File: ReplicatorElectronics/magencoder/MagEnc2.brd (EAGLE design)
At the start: 34.3 x 25.4 mm, 13 parts, among them J1 SBH11-PBPC-D07-ST-BK, J2 70553-0037, T1 MMBT2222A

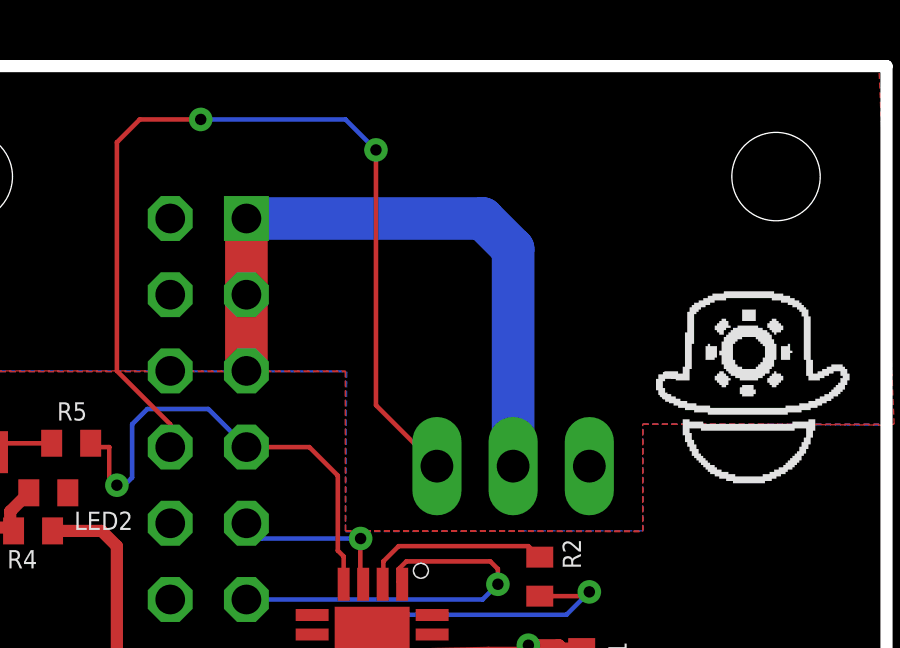
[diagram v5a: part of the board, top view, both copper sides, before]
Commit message: 2/10/13: Updated Encoder Board to include level translation. ~1 hour
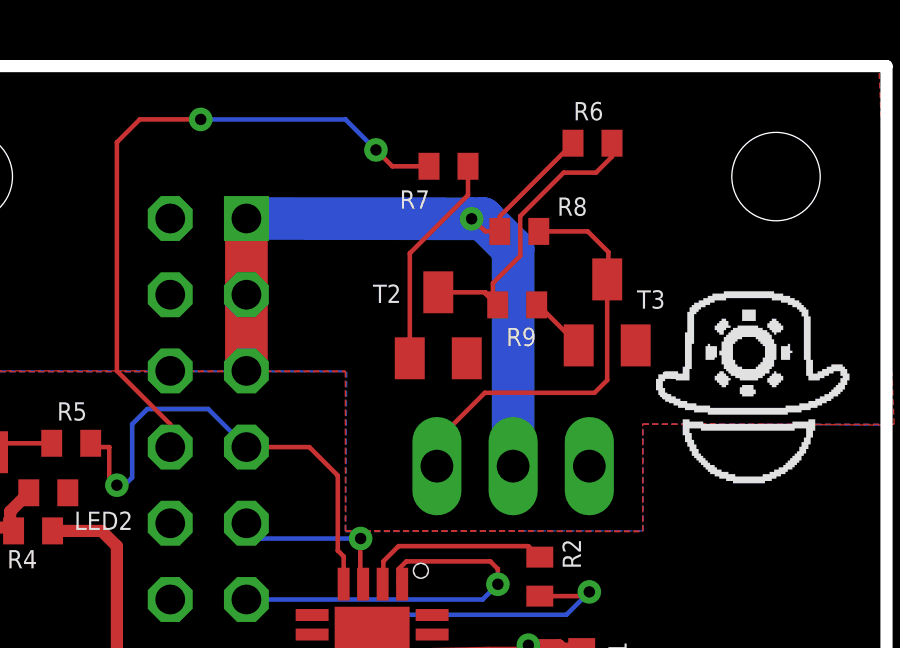
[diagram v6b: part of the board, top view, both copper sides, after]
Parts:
- added R6, R7, R8, R9: 1K, resistor:R0402
- added T2, T3: MMBT2222A, transistor:SOT23-BEC
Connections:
- new net 5V_SERVO_CTRL: J2.3, R8.2, T3.C
- new net CSN1: R6.2, R9.2, T2.C
- new net N$6: R7.1, T2.B
- new net N$8: R9.1, T3.B
- net 5V_SERVO: now also R6.1, R8.1
- net GND: now also T2.E, T3.E
- net SERVO_CTRL: now also R7.2; no longer J2.3
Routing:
- net 5V_SERVO_CTRL: track 0.00 -> 14.3 mm
- net CSN1: track 0.00 -> 10.3 mm
- net SERVO_CTRL: track 31.7 -> 22.3 mm
- net N$6: track 0.00 -> 7.22 mm
- net 5V_SERVO: track 21.6 -> 26.7 mm, vias 0 -> 1
- net N$8: track 0.00 -> 1.96 mm
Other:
- board text added: "Rev. 9"
- board text removed: "Rev. 8"
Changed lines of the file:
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@@
 <?xml version="1.0" encoding="utf-8"?>
 <!DOCTYPE eagle SYSTEM "eagle.dtd">
-<eagle version="6.2">
+<eagle version="6.1">
 <drawing>
 <settings>
@@
 <rectangle x1="27.178" y1="18.288" x2="34.29" y2="25.4" layer="42"/>
 <rectangle x1="27.178" y1="0" x2="34.29" y2="7.112" layer="42"/>
-<text x="28.448" y="9.017" size="0.6096" layer="101" font="vector">Rev. 8</text>
+<text x="28.448" y="9.017" size="0.6096" layer="101" font="vector">Rev. 9</text>
 <text x="25.273" y="8.128" size="0.6096" layer="101" font="vector">Francesco Bivona</text>
 <text x="44.069" y="6.096" size="0.6096" layer="101" font="vector">Mounting holes are 4-40 (0.116")</text>
@@
 <attribute name="NAME" x="24.892" y="3.429" size="0.6096" layer="25" font="vector" rot="R270"/>
 </element>
+<element name="T2" library="transistor" package="SOT23-BEC" value="MMBT2222A" x="19.35" y="16.76" smashed="yes">
+<attribute name="NAME" x="17.175" y="17.505" size="0.6096" layer="25" font="vector"/>
+</element>
+<element name="R6" library="resistor" package="R0402" value="1K" x="24.49" y="22.83" smashed="yes">
+<attribute name="NAME" x="23.855" y="23.592" size="0.6096" layer="25" font="vector"/>
+</element>
+<element name="R7" library="resistor" package="R0402" value="1K" x="19.69" y="22.06" smashed="yes" rot="R180">
+<attribute name="NAME" x="19.065" y="21.258" size="0.6096" layer="25" font="vector" rot="R180"/>
+</element>
+<element name="T3" library="transistor" package="SOT23-BEC" value="MMBT2222A" x="24.98" y="17.19" smashed="yes">
+<attribute name="NAME" x="25.975" y="17.315" size="0.6096" layer="25" font="vector"/>
+</element>
+<element name="R8" library="resistor" package="R0402" value="1K" x="22.05" y="19.89" smashed="yes">
+<attribute name="NAME" x="23.315" y="20.412" size="0.6096" layer="25" font="vector"/>
+</element>
+<element name="R9" library="resistor" package="R0402" value="1K" x="21.98" y="17.44" smashed="yes" rot="R180">
+<attribute name="NAME" x="22.615" y="16.678" size="0.6096" layer="25" font="vector" rot="R180"/>
+</element>
 </elements>
 <signals>
 <signal name="GND">
-<polygon width="0.1524" layer="1" isolate="0.254" rank="2">
+<polygon width="0.1524" layer="1" spacing="0.6096" isolate="0.254" rank="2">
 <vertex x="0.127" y="15.24"/>
 <vertex x="16.256" y="15.24"/>
@@
 <vertex x="34.29" y="25.273"/>
 </polygon>
+<contactref element="T2" pad="E"/>
+<contactref element="T3" pad="E"/>
 </signal>
 <signal name="VCC">
@@
 <wire x1="21.844" y1="12.065" x2="21.844" y2="19.304" width="1.4224" layer="16"/>
 <wire x1="21.844" y1="19.304" x2="20.828" y2="20.32" width="1.4224" layer="16"/>
-<wire x1="20.828" y1="20.32" x2="12.954" y2="20.32" width="1.4224" layer="16"/>
+<contactref element="R6" pad="1"/>
+<contactref element="R8" pad="1"/>
+<wire x1="20.828" y1="20.32" x2="20.46" y2="20.31" width="1.4224" layer="16"/>
+<wire x1="20.46" y1="20.31" x2="12.954" y2="20.32" width="1.4224" layer="16"/>
+<wire x1="21.4" y1="19.89" x2="21.4" y2="20.39" width="0.1524" layer="1"/>
+<wire x1="21.4" y1="20.39" x2="23.84" y2="22.83" width="0.1524" layer="1"/>
+<wire x1="21.4" y1="19.89" x2="20.92" y2="19.89" width="0.1524" layer="1"/>
+<wire x1="20.92" y1="19.89" x2="20.46" y2="20.31" width="0.1524" layer="1"/>
+<via x="20.46" y="20.31" extent="1-16" drill="0.381"/>
 </signal>
 <signal name="SERVO_CTRL">
-<contactref element="J2" pad="3"/>
 <contactref element="J1" pad="8"/>
 <wire x1="10.414" y1="12.7" x2="10.414" y2="13.462" width="0.1524" layer="1"/>
@@
 <wire x1="16.256" y1="23.622" x2="17.272" y2="22.606" width="0.1524" layer="16"/>
 <via x="17.272" y="22.606" extent="1-16" drill="0.381"/>
-<wire x1="17.272" y1="22.606" x2="17.272" y2="14.097" width="0.1524" layer="1"/>
-<wire x1="17.272" y1="14.097" x2="19.304" y2="12.065" width="0.1524" layer="1"/>
 <wire x1="8.636" y1="15.24" x2="10.414" y2="13.462" width="0.1524" layer="1"/>
+<contactref element="R7" pad="2"/>
+<wire x1="19.04" y1="22.06" x2="17.818" y2="22.06" width="0.1524" layer="1"/>
+<wire x1="17.818" y1="22.06" x2="17.272" y2="22.606" width="0.1524" layer="1"/>
 </signal>
 <signal name="DGND">
@@
 <wire x1="4.803" y1="12.827" x2="4.506" y2="12.53" width="0.1524" layer="1"/>
 </signal>
+<signal name="N$6">
+<contactref element="T2" pad="B"/>
+<contactref element="R7" pad="1"/>
+<wire x1="18.4" y1="15.66" x2="18.4" y2="19.16" width="0.1524" layer="1"/>
+<wire x1="18.4" y1="19.16" x2="20.34" y2="21.1" width="0.1524" layer="1"/>
+<wire x1="20.34" y1="21.1" x2="20.34" y2="22.06" width="0.1524" layer="1"/>
+<wire x1="20.34" y1="22.06" x2="20.35" y2="22.07" width="0.1524" layer="1"/>
+</signal>
+<signal name="CSN1">
+<contactref element="R9" pad="2"/>
+<contactref element="T2" pad="C"/>
+<contactref element="R6" pad="2"/>
+<wire x1="19.35" y1="17.86" x2="20.91" y2="17.86" width="0.1524" layer="1"/>
+<wire x1="20.91" y1="17.86" x2="21.33" y2="17.44" width="0.1524" layer="1"/>
+<wire x1="20.91" y1="17.86" x2="20.91" y2="17.83" width="0.1524" layer="1"/>
+<wire x1="20.91" y1="17.83" x2="21.17" y2="17.57" width="0.1524" layer="1"/>
+<wire x1="21.17" y1="17.57" x2="21.17" y2="18.16" width="0.1524" layer="1"/>
+<wire x1="21.17" y1="18.16" x2="22.08" y2="19.07" width="0.1524" layer="1"/>
+<wire x1="22.08" y1="19.07" x2="22.08" y2="20.4" width="0.1524" layer="1"/>
+<wire x1="22.08" y1="20.4" x2="23.53" y2="21.85" width="0.1524" layer="1"/>
+<wire x1="23.53" y1="21.85" x2="24.61" y2="21.85" width="0.1524" layer="1"/>
+<wire x1="24.61" y1="21.85" x2="25.14" y2="22.38" width="0.1524" layer="1"/>
+<wire x1="25.14" y1="22.38" x2="25.14" y2="22.8" width="0.1524" layer="1"/>
+<wire x1="25.14" y1="22.8" x2="25.21" y2="22.87" width="0.1524" layer="1"/>
+<wire x1="25.21" y1="22.87" x2="25.21" y2="22.82" width="0.1524" layer="1"/>
+<wire x1="25.21" y1="22.82" x2="25.22" y2="22.81" width="0.1524" layer="1"/>
+<wire x1="25.22" y1="22.81" x2="25.16" y2="22.81" width="0.1524" layer="1"/>
+<wire x1="25.16" y1="22.81" x2="25.14" y2="22.83" width="0.1524" layer="1"/>
+</signal>
+<signal name="5V_SERVO_CTRL">
+<contactref element="T3" pad="C"/>
+<contactref element="R8" pad="2"/>
+<contactref element="J2" pad="3"/>
+<wire x1="22.7" y1="19.89" x2="24.33" y2="19.89" width="0.1524" layer="1"/>
+<wire x1="24.33" y1="19.89" x2="25.02" y2="19.2" width="0.1524" layer="1"/>
+<wire x1="25.02" y1="19.2" x2="25.02" y2="18.33" width="0.1524" layer="1"/>
+<wire x1="25.02" y1="18.33" x2="24.98" y2="18.29" width="0.1524" layer="1"/>
+<wire x1="24.98" y1="18.29" x2="24.98" y2="14.93" width="0.1524" layer="1"/>
+<wire x1="24.98" y1="14.93" x2="24.56" y2="14.51" width="0.1524" layer="1"/>
+<wire x1="24.56" y1="14.51" x2="20.9" y2="14.51" width="0.1524" layer="1"/>
+<wire x1="20.9" y1="14.51" x2="19.31" y2="12.92" width="0.1524" layer="1"/>
+<wire x1="19.31" y1="12.92" x2="19.31" y2="12.071" width="0.1524" layer="1"/>
+<wire x1="19.31" y1="12.071" x2="19.304" y2="12.065" width="0.1524" layer="1"/>
+</signal>
+<signal name="N$8">
+<contactref element="T3" pad="B"/>
+<contactref element="R9" pad="1"/>
+<wire x1="22.63" y1="17.44" x2="22.68" y2="17.44" width="0.1524" layer="1"/>
+<wire x1="22.68" y1="17.44" x2="24.03" y2="16.09" width="0.1524" layer="1"/>
+</signal>
 </signals>
